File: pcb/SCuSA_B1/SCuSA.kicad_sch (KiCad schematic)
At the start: 78 parts, among them J101 USB4135-GF-A, J102 JST_S2B-PH-K-x, J103 Binding_Post_PKI_10_A_Au, J104 Binding_Post_PKI_10_A_Au, J105 SMA_Straight_Jack_Female, J107 77311-118-02LF, J108 77311-118-02LF, Q101 DMN2041LSD, SW101 JS202011CQN, SW102 JS202011CQN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

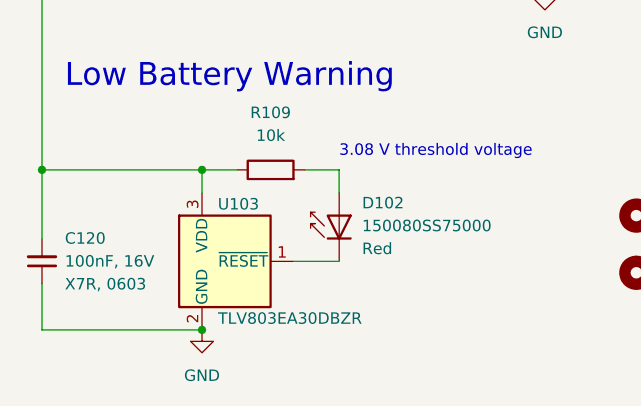
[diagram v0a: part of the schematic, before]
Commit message: Fix TLV803EA30DBZR (non-R pinout)
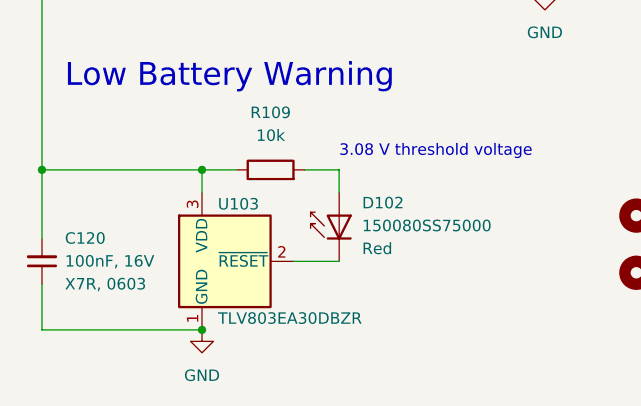
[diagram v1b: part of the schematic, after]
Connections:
- net GND: now also U103.1 (GND); no longer U103.2 (GND)
- net at D102.1 (K): now also U103.2 (~{RESET}); no longer U103.1 (~{RESET})

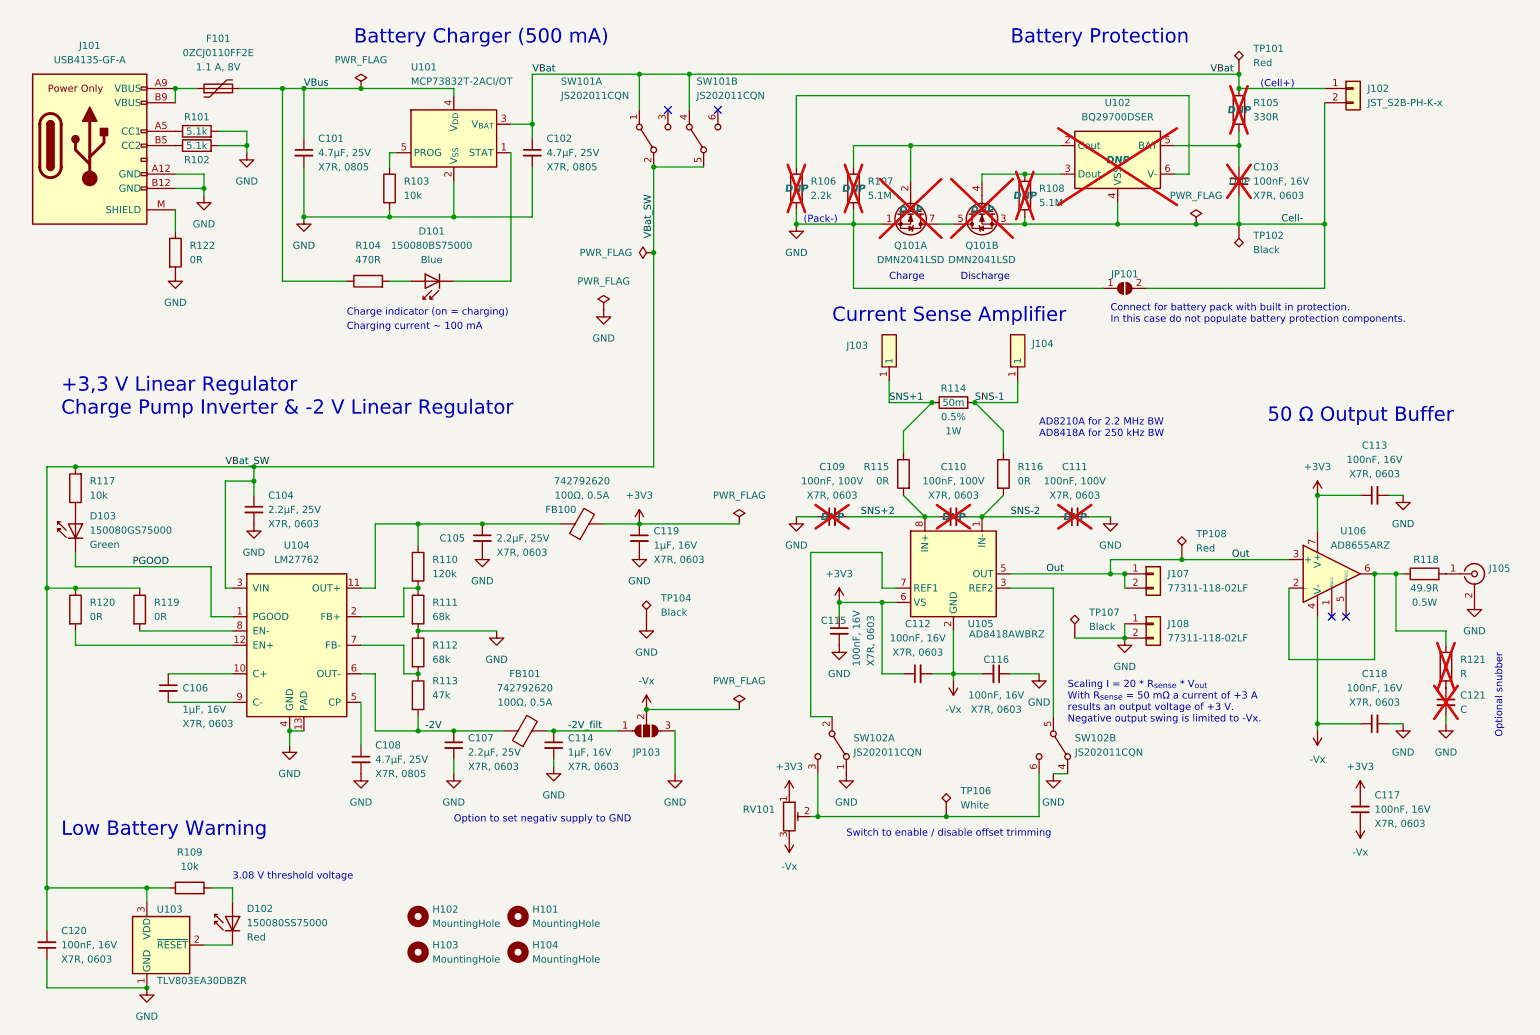
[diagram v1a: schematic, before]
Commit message: Change charge pump
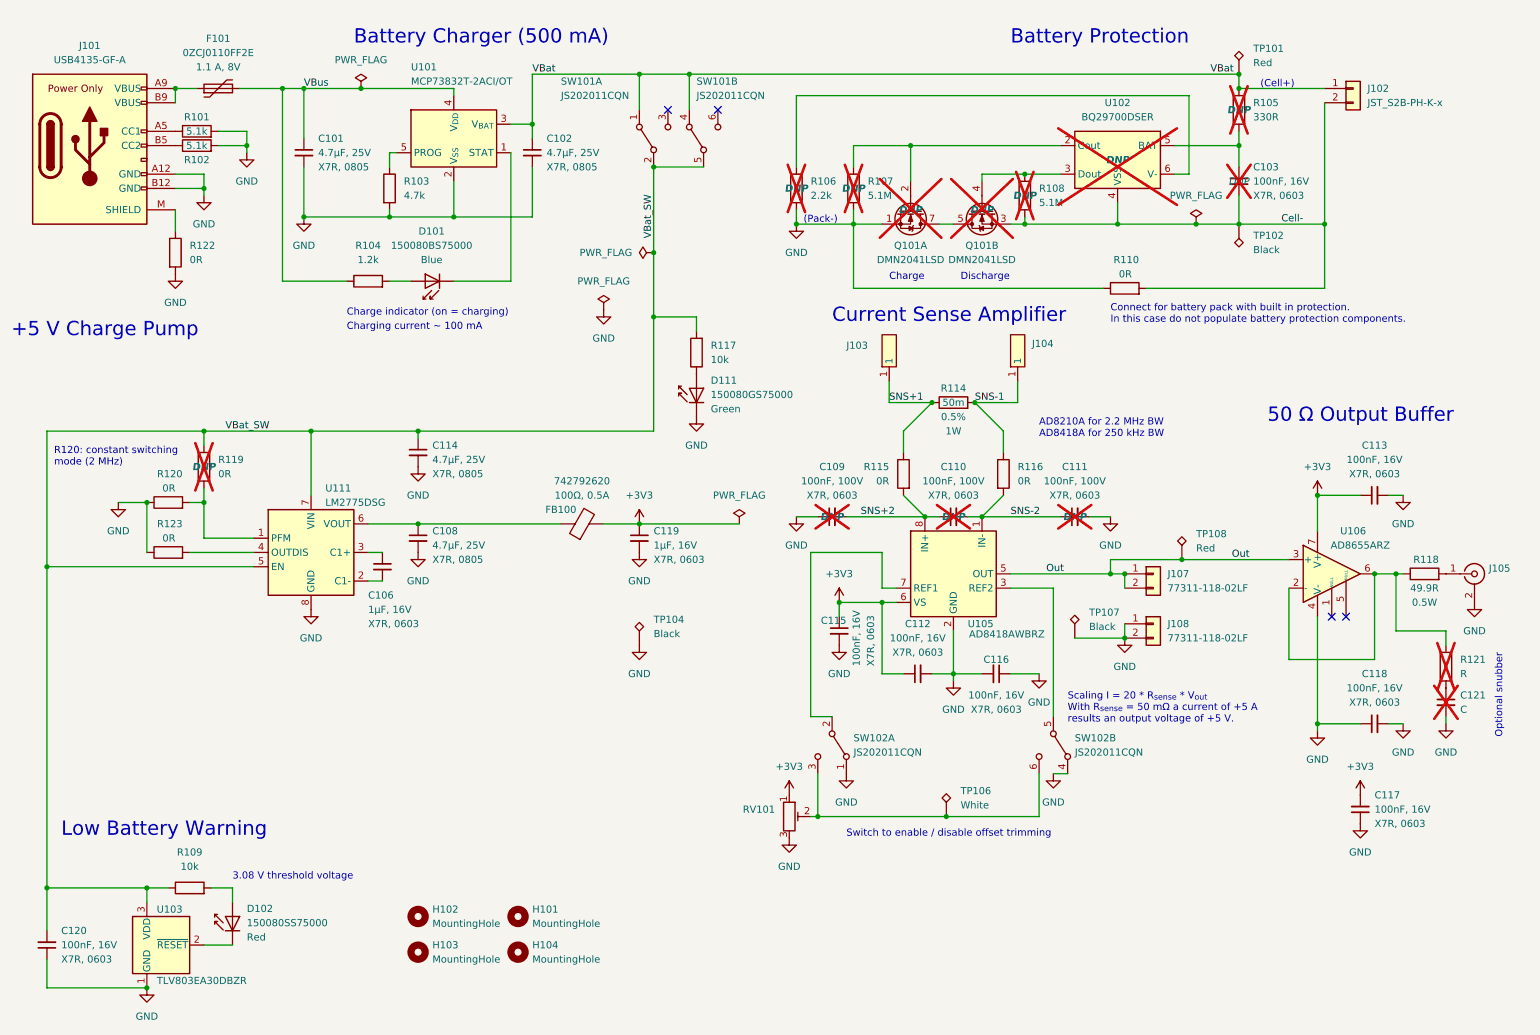
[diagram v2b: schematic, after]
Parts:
- removed C104, C105, C107: 2.2uF,25V,X7R,0603, Capacitor_SMD:C_0603_1608Metric_Pad1.08x0.95mm_HandSolder, symbol Capacitor_User:2.2uF,25V,X7R,0603
- removed C114: 1uF,16V,X7R,0603, Capacitor_SMD:C_0603_1608Metric_Pad1.08x0.95mm_HandSolder, symbol Capacitor_User:1uF,16V,X7R,0603
- removed D103: 150080GS75000, LED_SMD:LED_0805_2012Metric_Pad1.15x1.40mm_HandSolder, symbol LED_User:150080GS75000
- removed FB101: 742792620, Inductor_SMD:L_0603_1608Metric_Pad1.05x0.95mm_HandSolder, symbol Ferrite_User:742792620
- removed JP101: SolderJumper_2_Open, Jumper:SolderJumper-2_P1.3mm_Open_TrianglePad1.0x1.5mm, symbol Jumper:SolderJumper_2_Open
- removed JP103: SolderJumper_3_Open, Jumper:SolderJumper-3_P2.0mm_Open_TrianglePad1.0x1.5mm_NumberLabels, symbol Jumper:SolderJumper_3_Open
- removed R110: 120k,0603, Resistor_SMD:R_0603_1608Metric_Pad0.98x0.95mm_HandSolder, symbol Resistor_User:120k,0603
- removed R111, R112: 68k,0603, Resistor_SMD:R_0603_1608Metric_Pad0.98x0.95mm_HandSolder, symbol Resistor_User:68k,0603
- removed R113: 47k,0603, Resistor_SMD:R_0603_1608Metric_Pad0.98x0.95mm_HandSolder, symbol Resistor_User:47k,0603
- removed U104: LM27762, Package_SON_User:WSON-12-1EP_3x2mm_P0.5mm_EP1x2.65_ThermalVias, symbol Regulator_Switching_User:LM27762
- added C114: 4.7uF,25V,X7R,0805, Capacitor_SMD:C_0805_2012Metric_Pad1.18x1.45mm_HandSolder, symbol Capacitor_User:4.7uF,25V,X7R,0805
- added D111: 150080GS75000, LED_SMD:LED_0805_2012Metric_Pad1.15x1.40mm_HandSolder, symbol LED_User:150080GS75000
- added R110, R123: 0R,0603, Resistor_SMD:R_0603_1608Metric_Pad0.98x0.95mm_HandSolder, symbol Resistor_User:0R,0603
- added U111: LM2775DSG, Package_SON:WSON-8-1EP_2x2mm_P0.5mm_EP0.9x1.6mm_ThermalVias, symbol Regulator_SwitchedCapacitor:LM2775DSG
- R103: value 10k,0603 -> 4.7k,0603; symbol Resistor_User:10k,0603 -> Resistor_User:4.7k,0603; Resistance 10k -> 4.7k
- R104: value 470R,0603 -> 1.2k,0603; symbol Resistor_User:470R,0603 -> Resistor_User:1.2k,0603; Resistance 470R -> 1.2k
- R119: DNP (none) -> DNP; now not fitted
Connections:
- net -Vx is gone; now on net GND: C112.2, C116.2, C117.1, C118.1, RV101.3, U105.2 (GND), U106.4 (V-)
- net Cell-: now also R110.2
- net GND: now also R120.1, C114.2, D111.1 (K), R110.1, R123.1, U111.8 (GND), U111.9 (GND)
- net VBat_SW: now also C114.1, U111.5 (EN), U111.7 (VIN); no longer R120.1
- net at R120.2: now also R119.2, U111.1 (PFM)
- net at R117.1: now also D111.2 (A)
- net at FB100.1: now also C108.1, U111.6 (VOUT)
- net at C106.1: now also U111.3 (C1+)
- net at C106.2: now also U111.2 (C1-)
- new net: R123.2, U111.4 (OUTDIS)
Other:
- note added: "+5 V Charge Pump"
- note added: "R120: constant switching mode (2 MHz)"
- note added: "Scaling I = 20 * R_{sense} * V_{out} With R_{sense} = 50 mΩ a current of +5 A results an output voltage of +5 V."
- note removed: "+3,3 V Linear Regulator Charge Pump Inverter & -2 V Linear Regulator"
- note removed: "Option to set negativ supply to GND"
- note removed: "Scaling I = 20 * R_{sense} * V_{out} With R_{sense} = 50 mΩ a current of +3 A results an output voltage of +3 V. Negative output swing is limited to -Vx."
- moved on the sheet: C106, C108, R120, TP104

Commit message: Change voltage supervisor
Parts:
- removed U103: TLV803EA30DBZR, Package_TO_SOT_SMD:SOT-23, symbol Power_Supervisor_User:TLV803EA30DBZR
- added U103: BD4836G-xx, Package_TO_SOT_SMD:SOT-23-5, symbol Power_Supervisor_User:BD4836G-xx
- C119: value 1uF,16V,X7R,0603 -> 4.7uF,25V,X7R,0805; footprint Capacitor_SMD:C_0603_1608Metric_Pad1.08x0.95mm_HandSolder -> Capacitor_SMD:C_0805_2012Metric_Pad1.18x1.45mm_HandSolder; symbol Capacitor_User:1uF,16V,X7R,0603 -> Capacitor_User:4.7uF,25V,X7R,0805; Pretty Value 1 1μF, 16V -> 4.7μF, 25V; Pretty Value 2 X7R, 0603 -> X7R, 0805
- C120: DNP (none) -> DNP; now not fitted
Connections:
- net GND: now also U103.3 (GND)
- net VBat_SW: now also U103.2 (VDD)
- net at D102.1 (K): now also U103.1 (VOUT)
- net +3V3 renamed +5V
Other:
- note added: "3.6 V threshold voltage"
- note removed: "3.08 V threshold voltage"
- moved on the sheet: C119, D102, FB100, R109, TP104

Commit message: Edit PCB layout
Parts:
- removed TP101: TestPoint_5010_Red, TestPoint:TestPoint_Loop_D2.60mm_Drill1.6mm_Beaded, symbol Testpoint_User:TestPoint_5010_Red
- removed TP102, TP104: TestPoint_5011_Black, TestPoint:TestPoint_Loop_D2.60mm_Drill1.6mm_Beaded, symbol Testpoint_User:TestPoint_5011_Black
- removed TP106: TestPoint_5012_White, TestPoint:TestPoint_Loop_D2.60mm_Drill1.6mm_Beaded, symbol Testpoint_User:TestPoint_5012_White
- added unit 2 of J102
- J102: value JST_S2B-PH-K-x -> JST_S2B-PH-SM4-x; footprint Connector_JST:JST_PH_S2B-PH-K_1x02_P2.00mm_Horizontal -> Connector_User:JST_PH_S2B-PH-SM4-TB_1x02-1MP_P2.00mm_Horizontal; symbol Connector_User:JST_S2B-PH-K-x -> Connector_User:JST_S2B-PH-SM4-x; MPN S2B-PH-K-S -> S2B-PH-SM4-TB; SPN 455-1719-ND -> 455-S2B-PH-SM4-TBTR-ND
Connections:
- net GND: now also SW102.3 (C), SW102.6 (C), J102.MP; no longer SW102.1 (A), SW102.4 (A)
- new net: RV101.2, SW102.1 (A), SW102.4 (A)
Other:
- moved on the sheet: SW102A, SW102B

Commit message: Edit PCB layout
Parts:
- removed C117, C118: 100nF,16V,X7R,0603, Capacitor_SMD:C_0603_1608Metric_Pad1.08x0.95mm_HandSolder, symbol Capacitor_User:100nF,16V,X7R,0603
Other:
- moved on the sheet: C121, R121

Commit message: Edit PCB layout
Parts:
- removed R110: 0R,0603, Resistor_SMD:R_0603_1608Metric_Pad0.98x0.95mm_HandSolder, symbol Resistor_User:0R,0603
- added JP101: SolderJumper_2_Open, Jumper:SolderJumper-2_P1.3mm_Open_TrianglePad1.0x1.5mm, symbol Jumper:SolderJumper_2_Open
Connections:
- net Cell-: now also JP101.2 (B)
- net GND: now also JP101.1 (A)
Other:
- note added: "Close solder jumper for battery pack with built in protection. In this case do not populate battery protection components."
- note removed: "Connect for battery pack with built in protection. In this case do not populate battery protection components."
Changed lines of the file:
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@@
     (effects (font (size 1.27 1.27)) (justify left bottom))
   )
-  (text "Connect for battery pack with built in protection.\nIn this case do not populate battery protection components."
-    (at 213.36 69.85 0)
+  (text "Close solder jumper for battery pack with built in protection.\nIn this case do not populate battery protection components."
+    (at 212.09 69.85 0)
     (effects (font (size 1.27 1.27)) (justify left bottom))
   )
@@
     )
   )
+  (symbol (lib_id "Jumper:SolderJumper_2_Open") (at 215.9 63.5 0) (unit 1)
+    (in_bom yes) (on_board yes) (dnp no)
+    (property "Reference" "JP101" (at 215.9 60.96 0)
+      (effects (font (size 1.27 1.27)))
+    )
+    (property "Value" "SolderJumper_2_Open" (at 215.9 59.69 0)
+      (effects (font (size 1.27 1.27)) hide)
+    )
+    (property "Footprint" "Jumper:SolderJumper-2_P1.3mm_Open_TrianglePad1.0x1.5mm" (at 215.9 63.5 0)
+      (effects (font (size 1.27 1.27)) hide)
+    )
+    (property "Datasheet" "~" (at 215.9 63.5 0)
+      (effects (font (size 1.27 1.27)) hide)
+    )
+    (pin "1")
+    (pin "2")
+    (instances
+      (project "SCuSA"
+        (path "/7c524ebf-103a-4dc7-9ca9-e5a941b364b9"
+          (reference "JP101") (unit 1)
+        )
+      )
+    )
+  )
   (symbol (lib_id "Connector_User:Binding_Post_PKI_10_A_Au_Black") (at 196.85 77.47 90) (unit 1)
     (in_bom yes) (on_board yes) (dnp no)
@@
         )
       )
-    )
-  )
-  (symbol (lib_id "Resistor_User:0R,0603") (at 215.9 63.5 90) (unit 1)
-    (in_bom yes) (on_board yes) (dnp no)
-    (property "Reference" "R110" (at 218.44 58.42 90)
-      (effects (font (size 1.27 1.27)) (justify left))
-    )
-    (property "Value" "0R,0603" (at 213.36 61.595 0)
-      (effects (font (size 1.27 1.27)) (justify left) hide)
-    )
-    (property "Footprint" "Resistor_SMD:R_0603_1608Metric_Pad0.98x0.95mm_HandSolder" (at 226.06 60.96 0)
-      (effects (font (size 1.27 1.27)) hide)
-    )
-    (property "Datasheet" "~" (at 220.345 60.96 0)
-      (effects (font (size 1.27 1.27)) hide)
-    )
-    (property "Resistance" "0R" (at 217.17 60.96 90)
-      (effects (font (size 1.27 1.27)) (justify left))
-    )
-    (property "Tolerance" "1%" (at 215.9 58.42 0)
-      (effects (font (size 1.27 1.27)) (justify left) hide)
-    )
-    (property "Power" "0.1W" (at 215.9 52.705 0)
-      (effects (font (size 1.27 1.27)) hide)
-    )
-    (property "Package" "0603" (at 218.44 59.055 0)
-      (effects (font (size 1.27 1.27)) hide)
-    )
-    (pin "1")
-    (pin "2")
-    (instances
-      (project "SCuSA"
-        (path "/7c524ebf-103a-4dc7-9ca9-e5a941b364b9"
-          (reference "R110") (unit 1)
-        )
-      )
